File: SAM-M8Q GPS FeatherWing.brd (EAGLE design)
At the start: 50.8 x 22.9 mm, 25 parts, among them Q1 DMG3415U-7, Q2 2N2222, SW1 KMR2, U1 SAM-M8Q

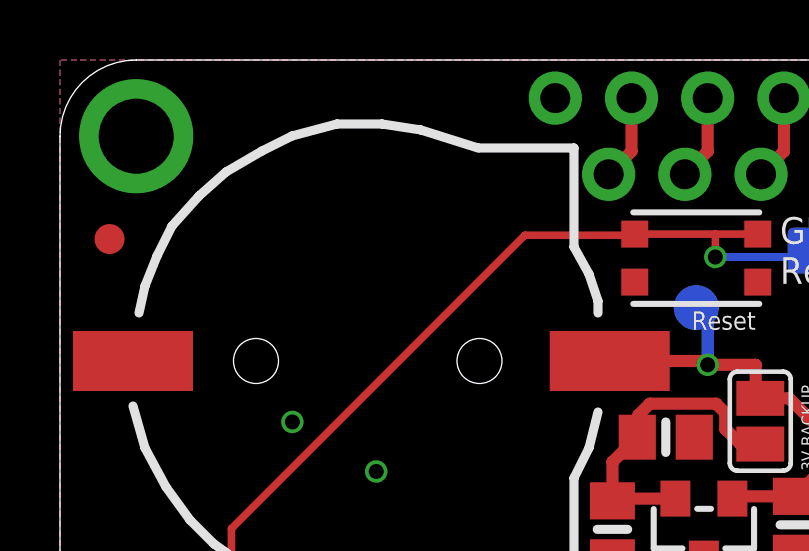
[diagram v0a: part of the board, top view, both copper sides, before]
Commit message: Minor tweaks. Included BOM.
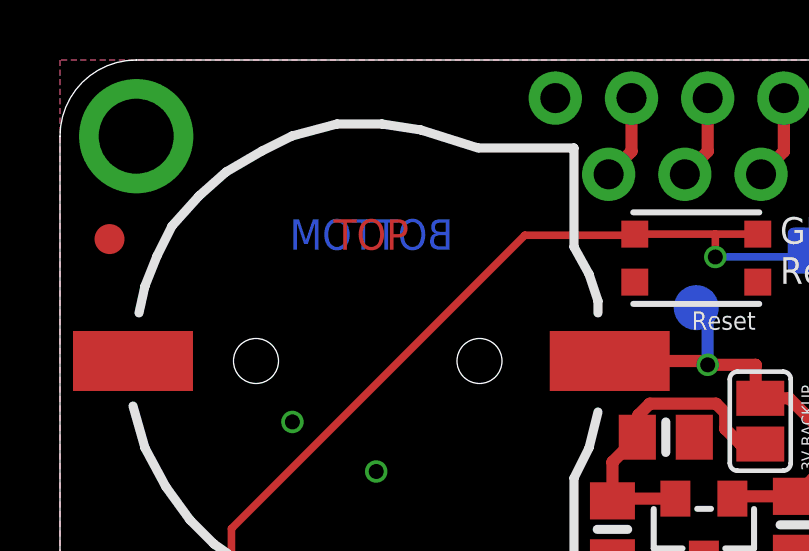
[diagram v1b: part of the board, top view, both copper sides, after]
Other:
- board text added: "B1"
- board text added: "BOTTOM"
- board text added: "C1"
- board text added: "C2"
- board text added: "FB1"
- board text added: "GRESET"
- board text added: "JP3"
- board text added: "LED1"
- board text added: "Q1"
- board text added: "Q2"
- board text added: "R1"
- board text added: "R2"
- board text added: "R3"
- board text added: "SW1"
- board text added: "TOP"
- board text added: "U1"
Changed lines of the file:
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@@
 <circle x="29.972" y="19.2532" radius="0.209453125" width="0.4064" layer="21"/>
 <text x="25.1206" y="9.1694" size="0.4064" layer="21" ratio="15" rot="R90">3V BACKUP</text>
+<text x="9.1186" y="16.5354" size="1.016" layer="1" ratio="15">TOP</text>
+<text x="13.1064" y="16.5354" size="1.016" layer="16" ratio="15" rot="MR0">BOTTOM</text>
+<text x="9.457946875" y="13.532103125" size="1.27" layer="51" ratio="12">B1</text>
+<text x="19.646140625" y="13.41475625" size="1.27" layer="51" ratio="12">SW1</text>
+<text x="19.236946875" y="11.176759375" size="1.27" layer="51" ratio="12">C2</text>
+<text x="17.475453125" y="5.6885875" size="1.27" layer="51" ratio="12" rot="R90">FB1</text>
+<text x="20.47036875" y="4.514340625" size="1.27" layer="51" ratio="12">Q1</text>
+<text x="27.756609375" y="8.818121875" size="1.27" layer="51" ratio="12" rot="R180">R2</text>
+<text x="26.419303125" y="4.088890625" size="1.27" layer="51" ratio="12">C1</text>
+<text x="37.148771875" y="11.00328125" size="1.27" layer="51" ratio="12">U1</text>
+<text x="47.3575375" y="13.745465625" size="1.27" layer="51" ratio="12">Q2</text>
+<text x="47.316390625" y="18.441159375" size="1.27" layer="51" ratio="12">R3</text>
+<text x="43.61383125" y="10.811259375" size="1.016" layer="51" ratio="12">LED1</text>
+<text x="45.002196875" y="8.72845625" size="1.27" layer="51" ratio="12">R1</text>
+<text x="46.76241875" y="4.3693125" size="1.27" layer="51" ratio="12">JP3</text>
+<text x="25.5778" y="14.9352" size="0.6096" layer="22" font="vector" ratio="14" rot="MR0" align="center">GRESET</text>
 </plain>
 <attributes>
